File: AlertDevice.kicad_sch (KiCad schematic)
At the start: 9 parts, among them Q35 2N2222, Q36 2N2222

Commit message: First try to fit electronic on PCB
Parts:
- renumbered D50 to D36, NT458 to NT470, Q35 to Q38, Q36 to Q39, R82 to R69, R83 to R70, R84 to R71, R85 to R72
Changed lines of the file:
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@@
   (symbol (lib_id "power:GND") (at 91.44 157.48 0) (unit 1)
     (in_bom yes) (on_board yes) (fields_autoplaced)
-    (property "Reference" "#PWR0134" (id 0) (at 91.44 163.83 0)
+    (property "Reference" "#PWR0122" (id 0) (at 91.44 163.83 0)
       (effects (font (size 1.27 1.27)) hide)
     )
@@
   (symbol (lib_id "Device:R_US") (at 78.74 148.59 270) (unit 1)
     (in_bom yes) (on_board yes)
-    (property "Reference" "R85" (id 0) (at 78.74 146.05 90))
+    (property "Reference" "R72" (id 0) (at 78.74 146.05 90))
     (property "Value" "10K" (id 1) (at 78.74 151.13 90))
     (property "Footprint" "Resistor_THT:R_Axial_DIN0309_L9.0mm_D3.2mm_P12.70mm_Horizontal" (id 2) (at 78.486 149.606 90)
@@
   (symbol (lib_id "Device:R_US") (at 83.82 49.53 180) (unit 1)
     (in_bom yes) (on_board yes)
-    (property "Reference" "R82" (id 0) (at 81.28 50.8 90))
+    (property "Reference" "R69" (id 0) (at 81.28 50.8 90))
     (property "Value" "220" (id 1) (at 86.36 49.53 90))
     (property "Footprint" "Resistor_THT:R_Axial_DIN0309_L9.0mm_D3.2mm_P12.70mm_Horizontal" (id 2) (at 82.804 49.276 90)
@@
   (symbol (lib_id "Device:R_US") (at 91.44 134.62 180) (unit 1)
     (in_bom yes) (on_board yes)
-    (property "Reference" "R84" (id 0) (at 86.36 135.89 0))
+    (property "Reference" "R71" (id 0) (at 86.36 135.89 0))
     (property "Value" "0" (id 1) (at 95.25 135.89 0))
     (property "Footprint" "Resistor_THT:R_Axial_DIN0309_L9.0mm_D3.2mm_P12.70mm_Horizontal" (id 2) (at 90.424 134.366 90)
@@
   (symbol (lib_id "power:VCC") (at 83.82 29.21 0) (unit 1)
     (in_bom yes) (on_board yes)
-    (property "Reference" "#PWR0131" (id 0) (at 83.82 33.02 0)
+    (property "Reference" "#PWR0119" (id 0) (at 83.82 33.02 0)
       (effects (font (size 1.27 1.27)) hide)
     )
@@
   (symbol (lib_id "Device:R_US") (at 71.12 64.77 270) (unit 1)
     (in_bom yes) (on_board yes)
-    (property "Reference" "R83" (id 0) (at 71.12 62.23 90))
+    (property "Reference" "R70" (id 0) (at 71.12 62.23 90))
     (property "Value" "10K" (id 1) (at 71.12 67.31 90))
     (property "Footprint" "Resistor_THT:R_Axial_DIN0309_L9.0mm_D3.2mm_P12.70mm_Horizontal" (id 2) (at 70.866 65.786 90)
@@
   (symbol (lib_id "Device:LED") (at 83.82 35.56 90) (unit 1)
     (in_bom yes) (on_board yes)
-    (property "Reference" "D50" (id 0) (at 86.36 34.29 90)
+    (property "Reference" "D36" (id 0) (at 86.36 34.29 90)
       (effects (font (size 1.27 1.27)) (justify right))
     )
@@
   (symbol (lib_id "power:GND") (at 83.82 73.66 0) (unit 1)
     (in_bom yes) (on_board yes) (fields_autoplaced)
-    (property "Reference" "#PWR0132" (id 0) (at 83.82 80.01 0)
+    (property "Reference" "#PWR0120" (id 0) (at 83.82 80.01 0)
       (effects (font (size 1.27 1.27)) hide)
     )
@@
   (symbol (lib_id "Device:NetTie_2") (at 88.9 57.15 0) (unit 1)
     (in_bom yes) (on_board yes)
-    (property "Reference" "NT458" (id 0) (at 88.9 55.88 0))
+    (property "Reference" "NT470" (id 0) (at 88.9 55.88 0))
     (property "Value" "ERR_L" (id 1) (at 88.9 58.42 0))
     (property "Footprint" "NetTie:NetTie-2_THT_Pad1.0mm" (id 2) (at 88.9 57.15 0)
@@
   (symbol (lib_id "Transistor_BJT:2N3904") (at 88.9 148.59 0) (unit 1)
     (in_bom yes) (on_board yes)
-    (property "Reference" "Q36" (id 0) (at 85.09 151.13 0))
+    (property "Reference" "Q39" (id 0) (at 85.09 151.13 0))
     (property "Value" "2N2222" (id 1) (at 85.09 153.67 0))
     (property "Footprint" "Package_TO_SOT_THT:TO-92_Inline" (id 2) (at 93.98 150.495 0)
@@
   (symbol (lib_id "Transistor_BJT:2N3904") (at 81.28 64.77 0) (unit 1)
     (in_bom yes) (on_board yes)
-    (property "Reference" "Q35" (id 0) (at 77.47 67.31 0))
+    (property "Reference" "Q38" (id 0) (at 77.47 67.31 0))
     (property "Value" "2N2222" (id 1) (at 77.47 69.85 0))
     (property "Footprint" "Package_TO_SOT_THT:TO-92_Inline" (id 2) (at 86.36 66.675 0)
@@
   (symbol (lib_id "power:VCC") (at 91.44 111.76 0) (unit 1)
     (in_bom yes) (on_board yes)
-    (property "Reference" "#PWR0133" (id 0) (at 91.44 115.57 0)
+    (property "Reference" "#PWR0121" (id 0) (at 91.44 115.57 0)
       (effects (font (size 1.27 1.27)) hide)
     )

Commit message: backup 1 bank done
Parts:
- removed Q38, Q39: 2N2222, Package_TO_SOT_THT:TO-92_Inline, symbol Transistor_BJT:2N3904
- removed R70, R72: 10K, Resistor_THT:R_Axial_DIN0309_L9.0mm_D3.2mm_P12.70mm_Horizontal, symbol Device:R_US
- NT470: footprint NetTie:NetTie-2_THT_Pad1.0mm -> NetTie:NetTie-2_Front1.0mm
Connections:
- net BEEP_D: now reaches R71.1
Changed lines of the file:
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@@
+    (stroke (width 0) (type default) (color 0 0 0 0))
+  )
+  (wire (pts (xy 68.58 64.77) (xy 83.82 64.77))
     (stroke (width 0) (type default) (color 0 0 0 0))
   )
@@
     (stroke (width 0) (type default) (color 0 0 0 0))
   )
-  (wire (pts (xy 91.44 138.43) (xy 91.44 143.51))
-    (stroke (width 0) (type default) (color 0 0 0 0))
-  )
-  (wire (pts (xy 82.55 148.59) (xy 83.82 148.59))
-    (stroke (width 0) (type default) (color 0 0 0 0))
-  )
-  (wire (pts (xy 91.44 153.67) (xy 91.44 157.48))
-    (stroke (width 0) (type default) (color 0 0 0 0))
-  )
   (wire (pts (xy 91.44 57.15) (xy 102.87 57.15))
     (stroke (width 0) (type default) (color 0 0 0 0))
   )
+  (wire (pts (xy 91.44 138.43) (xy 91.44 148.59))
+    (stroke (width 0) (type default) (color 0 0 0 0))
+  )
   (wire (pts (xy 83.82 29.21) (xy 83.82 31.75))
     (stroke (width 0) (type default) (color 0 0 0 0))
   )
-  (wire (pts (xy 67.31 148.59) (xy 74.93 148.59))
-    (stroke (width 0) (type default) (color 0 0 0 0))
-  )
-  (wire (pts (xy 74.93 64.77) (xy 76.2 64.77))
+  (wire (pts (xy 67.31 148.59) (xy 91.44 148.59))
     (stroke (width 0) (type default) (color 0 0 0 0))
   )
@@
     (stroke (width 0) (type default) (color 0 0 0 0))
   )
-  (wire (pts (xy 83.82 69.85) (xy 83.82 73.66))
-    (stroke (width 0) (type default) (color 0 0 0 0))
-  )
-  (wire (pts (xy 83.82 57.15) (xy 83.82 59.69))
+  (wire (pts (xy 83.82 57.15) (xy 83.82 64.77))
     (stroke (width 0) (type default) (color 0 0 0 0))
   )
@@
     (effects (font (size 1.27 1.27)) (justify left bottom))
   )
-  (global_label "BEEPER" (shape input) (at 67.31 148.59 180) (fields_autoplaced)
+  (global_label "BEEP_D" (shape input) (at 67.31 148.59 180) (fields_autoplaced)
     (effects (font (size 1.27 1.27)) (justify right))
-    (property "Intersheet References" "${INTERSHEET_REFS}" (id 0) (at 57.6398 148.5106 0)
+    (property "Intersheet References" "${INTERSHEET_REFS}" (id 0) (at 57.8212 148.5106 0)
       (effects (font (size 1.27 1.27)) (justify right) hide)
     )
   )
-  (global_label "ERROR_LED" (shape input) (at 59.69 64.77 180) (fields_autoplaced)
+  (global_label "ERR_LED_D" (shape input) (at 59.69 64.77 180) (fields_autoplaced)
     (effects (font (size 1.27 1.27)) (justify right))
-    (property "Intersheet References" "${INTERSHEET_REFS}" (id 0) (at 46.5726 64.6906 0)
+    (property "Intersheet References" "${INTERSHEET_REFS}" (id 0) (at 46.9355 64.6906 0)
       (effects (font (size 1.27 1.27)) (justify right) hide)
     )
@@
       (effects (font (size 1.27 1.27)) (justify left) hide)
     )
-  )
-  (symbol (lib_id "power:GND") (at 91.44 157.48 0) (unit 1)
-    (in_bom yes) (on_board yes) (fields_autoplaced)
-    (property "Reference" "#PWR0122" (id 0) (at 91.44 163.83 0)
-      (effects (font (size 1.27 1.27)) hide)
-    )
-    (property "Value" "GND" (id 1) (at 91.44 162.56 0))
-    (property "Footprint" "" (id 2) (at 91.44 157.48 0)
-      (effects (font (size 1.27 1.27)) hide)
-    )
-    (property "Datasheet" "" (id 3) (at 91.44 157.48 0)
-      (effects (font (size 1.27 1.27)) hide)
-    )
-    (pin "1")
-  )
-  (symbol (lib_id "Device:R_US") (at 78.74 148.59 270) (unit 1)
-    (in_bom yes) (on_board yes)
-    (property "Reference" "R72" (id 0) (at 78.74 146.05 90))
-    (property "Value" "10K" (id 1) (at 78.74 151.13 90))
-    (property "Footprint" "Resistor_THT:R_Axial_DIN0309_L9.0mm_D3.2mm_P12.70mm_Horizontal" (id 2) (at 78.486 149.606 90)
-      (effects (font (size 1.27 1.27)) hide)
-    )
-    (property "Datasheet" "~" (id 3) (at 78.74 148.59 0)
-      (effects (font (size 1.27 1.27)) hide)
-    )
-    (pin "1")
-    (pin "2")
   )
   (symbol (lib_id "Device:R_US") (at 83.82 49.53 180) (unit 1)
@@
     (pin "1")
   )
-  (symbol (lib_id "Device:R_US") (at 71.12 64.77 270) (unit 1)
-    (in_bom yes) (on_board yes)
-    (property "Reference" "R70" (id 0) (at 71.12 62.23 90))
-    (property "Value" "10K" (id 1) (at 71.12 67.31 90))
-    (property "Footprint" "Resistor_THT:R_Axial_DIN0309_L9.0mm_D3.2mm_P12.70mm_Horizontal" (id 2) (at 70.866 65.786 90)
-      (effects (font (size 1.27 1.27)) hide)
-    )
-    (property "Datasheet" "~" (id 3) (at 71.12 64.77 0)
-      (effects (font (size 1.27 1.27)) hide)
-    )
-    (pin "1")
-    (pin "2")
-  )
   (symbol (lib_id "Device:LED") (at 83.82 35.56 90) (unit 1)
     (in_bom yes) (on_board yes)
@@
     (pin "2")
   )
-  (symbol (lib_id "power:GND") (at 83.82 73.66 0) (unit 1)
-    (in_bom yes) (on_board yes) (fields_autoplaced)
-    (property "Reference" "#PWR0120" (id 0) (at 83.82 80.01 0)
-      (effects (font (size 1.27 1.27)) hide)
-    )
-    (property "Value" "GND" (id 1) (at 83.82 78.74 0))
-    (property "Footprint" "" (id 2) (at 83.82 73.66 0)
-      (effects (font (size 1.27 1.27)) hide)
-    )
-    (property "Datasheet" "" (id 3) (at 83.82 73.66 0)
-      (effects (font (size 1.27 1.27)) hide)
-    )
-    (pin "1")
-  )
   (symbol (lib_id "Device:NetTie_2") (at 88.9 57.15 0) (unit 1)
     (in_bom yes) (on_board yes)
     (property "Reference" "NT470" (id 0) (at 88.9 55.88 0))
     (property "Value" "ERR_L" (id 1) (at 88.9 58.42 0))
-    (property "Footprint" "NetTie:NetTie-2_THT_Pad1.0mm" (id 2) (at 88.9 57.15 0)
+    (property "Footprint" "NetTie:NetTie-2_Front1.0mm" (id 2) (at 88.9 57.15 0)
       (effects (font (size 1.27 1.27)) hide)
     )
@@
     (pin "2")
   )
-  (symbol (lib_id "Transistor_BJT:2N3904") (at 88.9 148.59 0) (unit 1)
-    (in_bom yes) (on_board yes)
-    (property "Reference" "Q39" (id 0) (at 85.09 151.13 0))
-    (property "Value" "2N2222" (id 1) (at 85.09 153.67 0))
-    (property "Footprint" "Package_TO_SOT_THT:TO-92_Inline" (id 2) (at 93.98 150.495 0)
-      (effects (font (size 1.27 1.27) italic) (justify left) hide)
-    )
-    (property "Datasheet" "https://www.onsemi.com/pub/Collateral/2N3903-D.PDF" (id 3) (at 88.9 148.59 0)
-      (effects (font (size 1.27 1.27)) (justify left) hide)
-    )
-    (pin "1")
-    (pin "2")
-    (pin "3")
-  )
-  (symbol (lib_id "Transistor_BJT:2N3904") (at 81.28 64.77 0) (unit 1)
-    (in_bom yes) (on_board yes)
-    (property "Reference" "Q38" (id 0) (at 77.47 67.31 0))
-    (property "Value" "2N2222" (id 1) (at 77.47 69.85 0))
-    (property "Footprint" "Package_TO_SOT_THT:TO-92_Inline" (id 2) (at 86.36 66.675 0)
-      (effects (font (size 1.27 1.27) italic) (justify left) hide)
-    )
-    (property "Datasheet" "https://www.onsemi.com/pub/Collateral/2N3903-D.PDF" (id 3) (at 81.28 64.77 0)
-      (effects (font (size 1.27 1.27)) (justify left) hide)
-    )
-    (pin "1")
-    (pin "2")
-    (pin "3")
-  )
   (symbol (lib_id "power:VCC") (at 91.44 111.76 0) (unit 1)

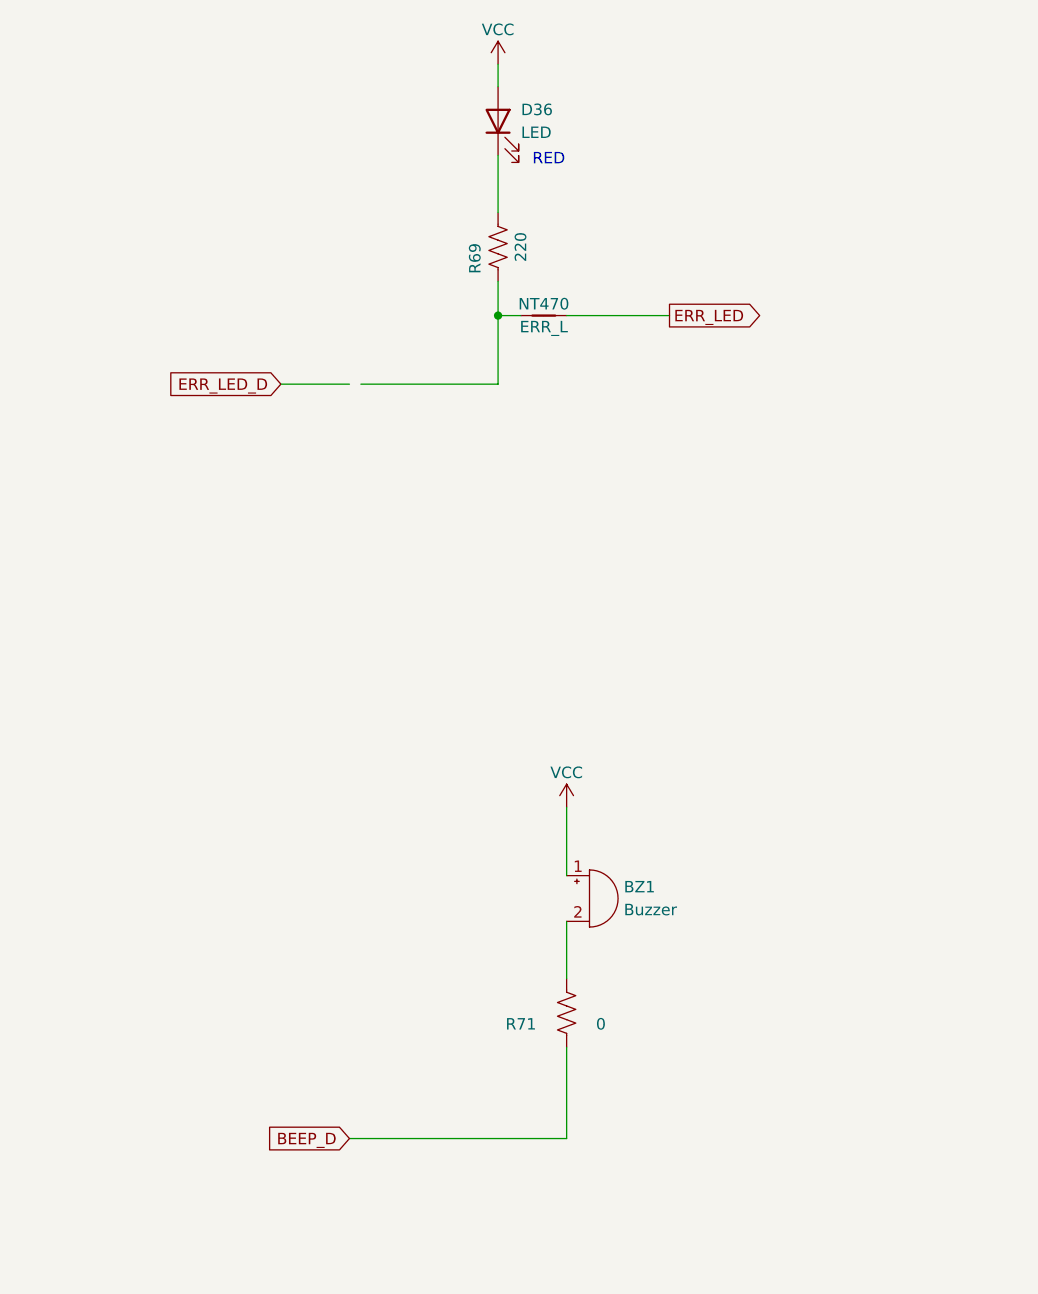
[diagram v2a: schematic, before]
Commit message: half PCB completed
FTS io controller PCB
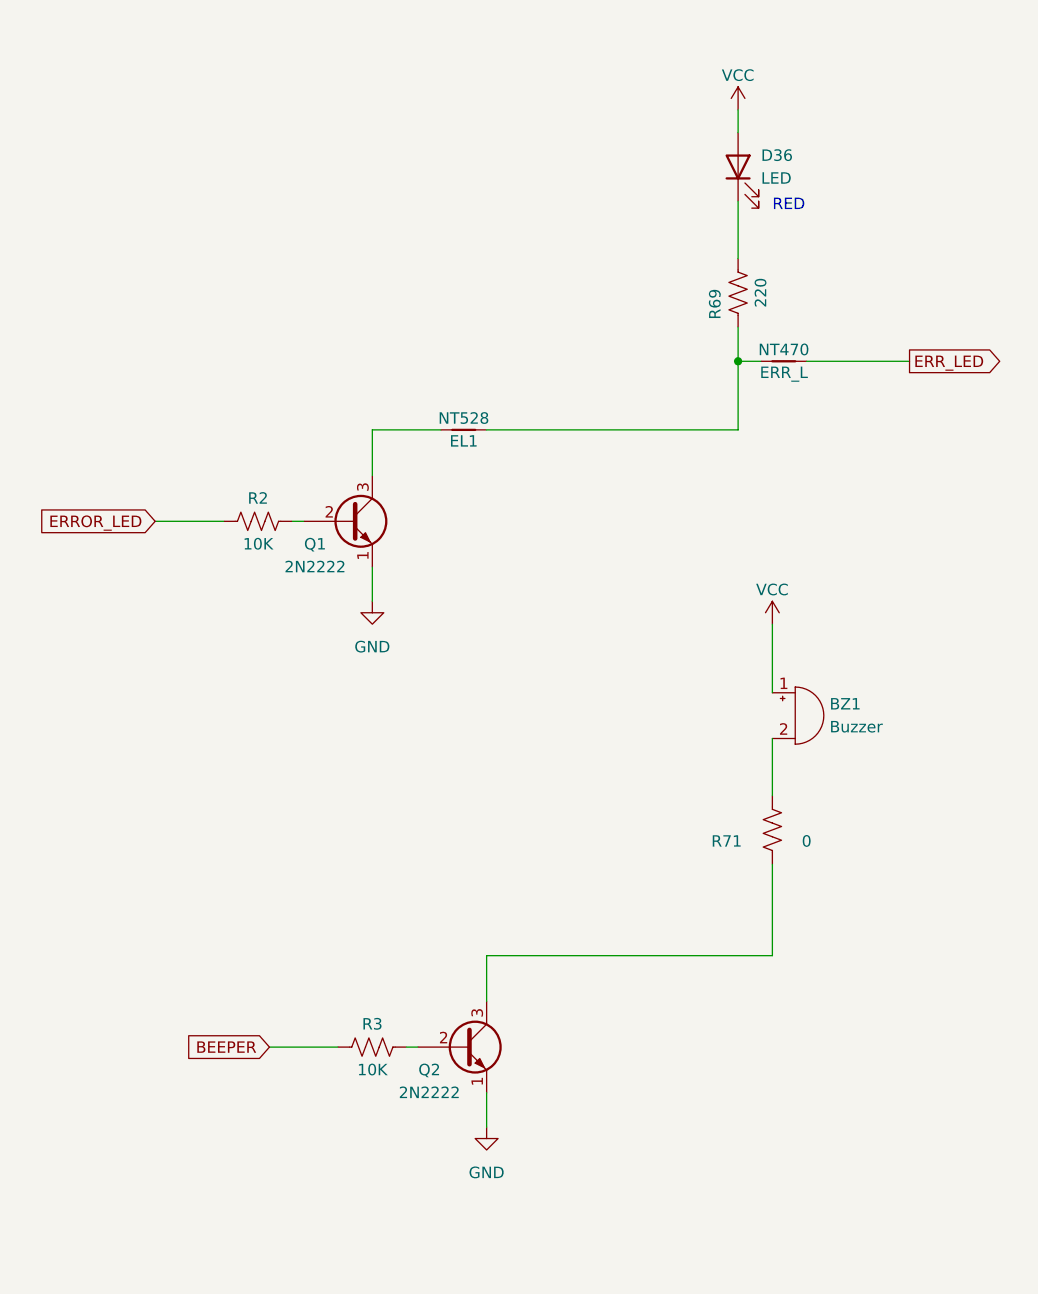
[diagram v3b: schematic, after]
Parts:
- added NT528: EL1, NetTie:NetTie-2_Front1.0mm, symbol Device:NetTie_2
- added Q1, Q2: 2N2222, Package_TO_SOT_THT:TO-92_Inline, symbol Transistor_BJT:2N3904
- added R2, R3: 10K, Resistor_THT:R_Axial_DIN0309_L9.0mm_D3.2mm_P12.70mm_Horizontal, symbol Device:R_US
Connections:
- net at NT470.1, R69.1: now also NT528.2
- net BEEP_D: no longer names the net of R71.1
- net BEEP_D: now also Q2.3 (C)
- new net: Q2.2 (B), R3.1
- new net: Q1.2 (B), R2.1
- new net: NT528.1, Q1.3 (C)
- new net BEEPER: R3.2
- new net ERROR_LED: R2.2
- new net GND: Q1.1 (E), Q2.1 (E)
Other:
- moved on the sheet: BZ1, D36, NT470, R69, R71

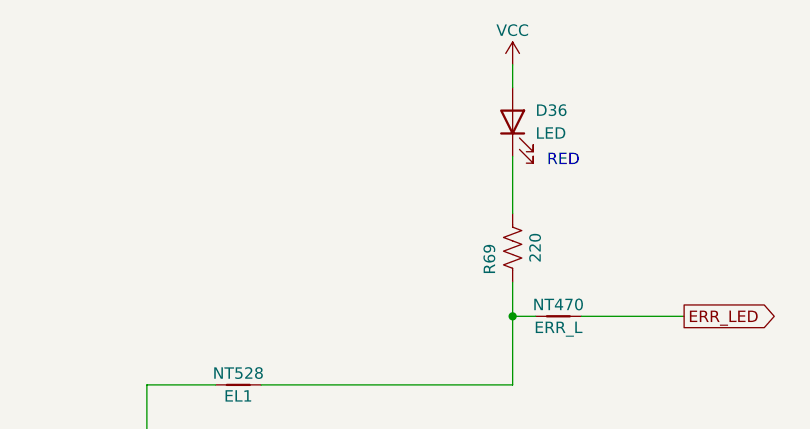
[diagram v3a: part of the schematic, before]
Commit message: PCB Completed
PCB completed but final verification not completed
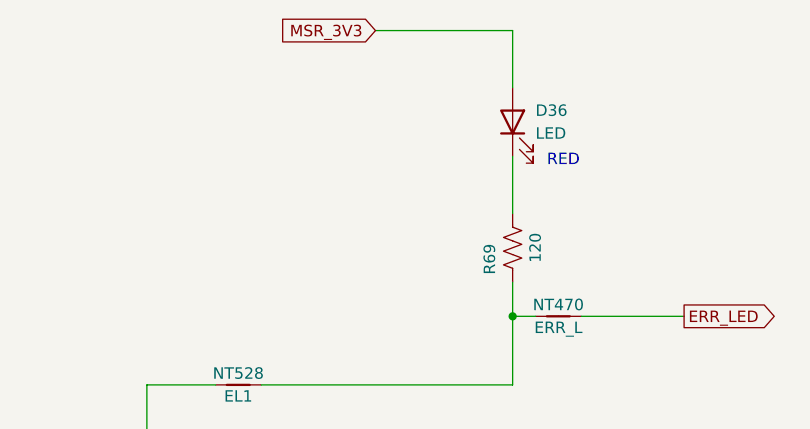
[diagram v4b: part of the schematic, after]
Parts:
- R69: value 220 -> 120
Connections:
- net VCC: no longer D36.2 (A)
- new net MSR_3V3: D36.2 (A)
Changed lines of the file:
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@@
     (stroke (width 0) (type default) (color 0 0 0 0))
   )
-  (wire (pts (xy 110.49 34.29) (xy 110.49 36.83))
+  (wire (pts (xy 110.49 30.48) (xy 110.49 36.83))
     (stroke (width 0) (type default) (color 0 0 0 0))
   )
@@
   )
   (wire (pts (xy 45.72 80.01) (xy 53.34 80.01))
+    (stroke (width 0) (type default) (color 0 0 0 0))
+  )
+  (wire (pts (xy 95.25 30.48) (xy 110.49 30.48))
     (stroke (width 0) (type default) (color 0 0 0 0))
   )
@@
     (effects (font (size 1.27 1.27)) (justify left bottom))
   )
+  (global_label "MSR_3V3" (shape input) (at 95.25 30.48 180) (fields_autoplaced)
+    (effects (font (size 1.27 1.27)) (justify right))
+    (property "Intersheet References" "${INTERSHEET_REFS}" (id 0) (at 84.4307 30.4006 0)
+      (effects (font (size 1.27 1.27)) (justify right) hide)
+    )
+  )
   (global_label "BEEPER" (shape input) (at 58.42 138.43 180) (fields_autoplaced)
     (effects (font (size 1.27 1.27)) (justify right))
@@
     (in_bom yes) (on_board yes)
     (property "Reference" "R69" (id 0) (at 107.95 55.88 90))
-    (property "Value" "220" (id 1) (at 113.03 54.61 90))
+    (property "Value" "120" (id 1) (at 113.03 54.61 90))
     (property "Footprint" "Resistor_THT:R_Axial_DIN0309_L9.0mm_D3.2mm_P12.70mm_Horizontal" (id 2) (at 109.474 54.356 90)
       (effects (font (size 1.27 1.27)) hide)
@@
     (pin "2")
   )
-  (symbol (lib_id "power:VCC") (at 110.49 34.29 0) (unit 1)
-    (in_bom yes) (on_board yes)
-    (property "Reference" "#PWR0119" (id 0) (at 110.49 38.1 0)
-      (effects (font (size 1.27 1.27)) hide)
-    )
-    (property "Value" "VCC" (id 1) (at 110.49 30.48 0))
-    (property "Footprint" "" (id 2) (at 110.49 34.29 0)
-      (effects (font (size 1.27 1.27)) hide)
-    )
-    (property "Datasheet" "" (id 3) (at 110.49 34.29 0)
-      (effects (font (size 1.27 1.27)) hide)
-    )
-    (pin "1")
-  )
   (symbol (lib_id "Device:R_US") (at 57.15 80.01 270) (unit 1)
